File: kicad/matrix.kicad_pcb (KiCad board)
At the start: 2 copper layers, 110.7 x 76.2 mm, 20 parts, among them J1 Conn_01x08, U1 TLC59025, U10 P-FET, U11 P-FET, U2 74HC595, U3 74HC595, U4 P-FET, U5 P-FET, U6 P-FET, U7 P-FET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

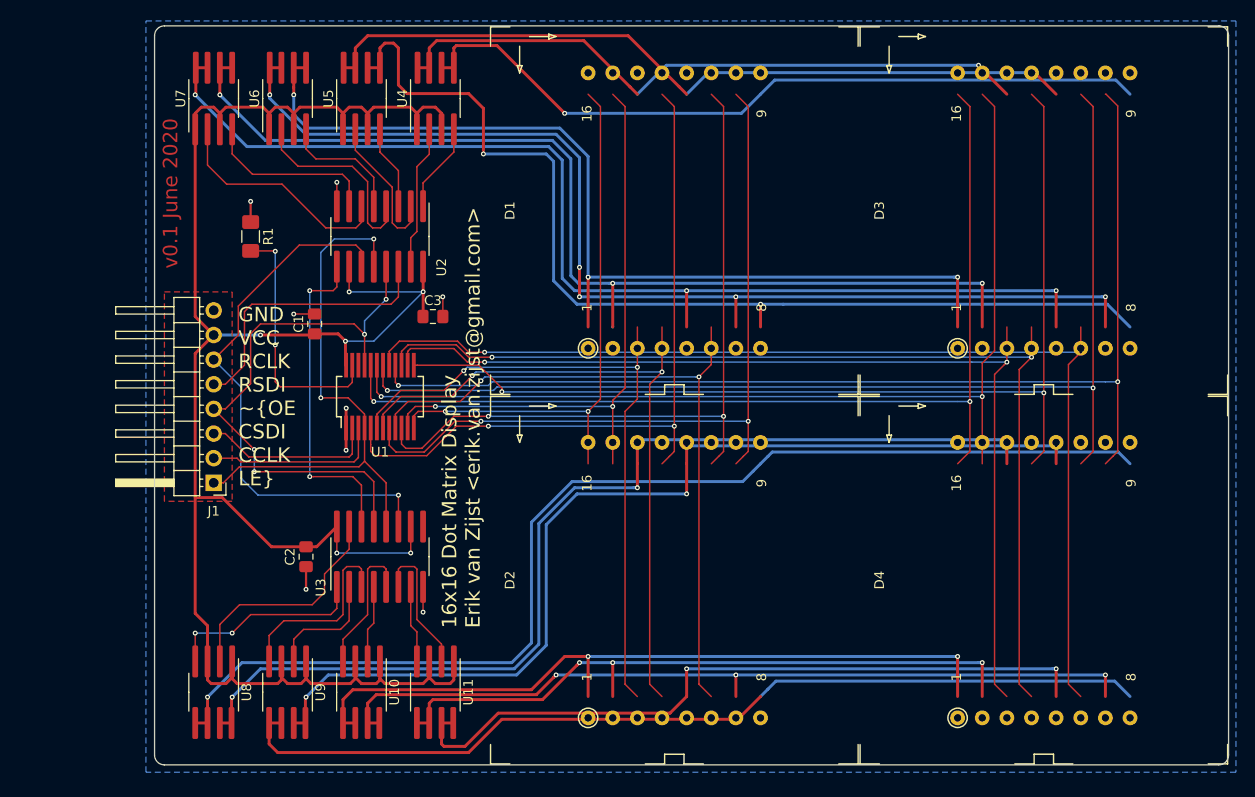
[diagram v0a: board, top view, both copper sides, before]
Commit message: Resize board and place components
Routing up next.
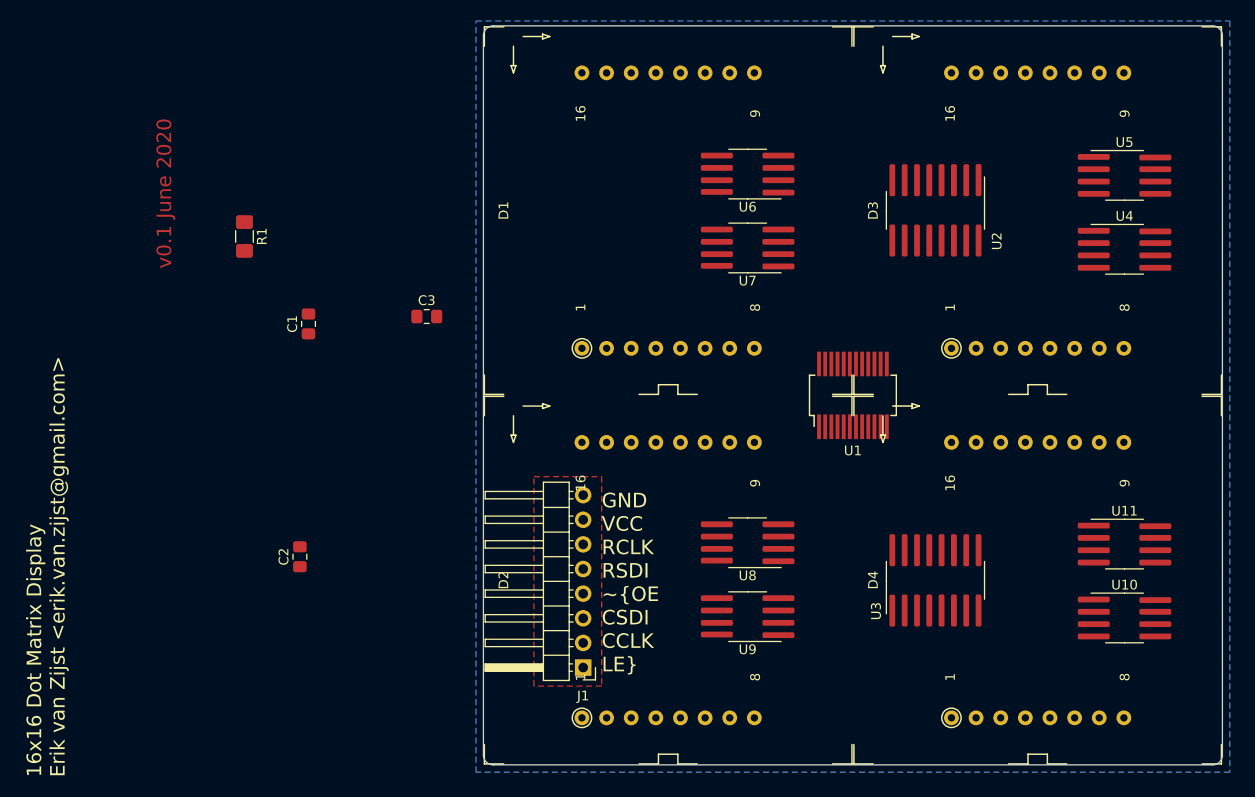
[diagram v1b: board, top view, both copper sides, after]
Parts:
- moved U5 79.1 mm to (218.4, 52.8), turned to 0 degrees
- moved U10 79.1 mm to (218.4, 98.4), turned to 0 degrees
- moved U4 72.7 mm to (218.4, 60.4), turned to 0 degrees
- moved U11 72.7 mm to (218.4, 90.8), turned to 0 degrees
- moved U2 57.3 mm to (198.9, 56.4)
- moved U3 57.3 mm to (198.9, 94.5)
- moved U7 57.2 mm to (179.5, 60.2), turned to 180 degrees
- moved U8 57.2 mm to (179.5, 90.6), turned to 180 degrees
- moved U1 48.8 mm to (190.4, 75.4)
- moved U6 48.1 mm to (179.5, 52.6), turned to 180 degrees
- moved U9 48.1 mm to (179.5, 98.3), turned to 180 degrees
- moved J1 42.6 mm to (162.6, 103.5)
- moved C2 0.64 mm to (133.3, 92.1)
- moved R1 0.64 mm to (127.6, 59.1)
- moved C1 0.63 mm to (134.2, 68.1)
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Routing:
- net VDD: track 223.1 -> 0.00 mm, vias 6 -> 0
- net /ROW9: track 117.3 -> 0.00 mm, vias 1 -> 0
- net /ROW8: track 115.8 -> 0.00 mm, vias 3 -> 0
- net /COL11: track 115.7 -> 0.00 mm, vias 2 -> 0
- net /COL13: track 114.9 -> 0.00 mm, vias 2 -> 0
- net /ROW6: track 113.6 -> 0.00 mm, vias 5 -> 0
- net /COL12: track 112.8 -> 0.00 mm, vias 2 -> 0
- net /ROW3: track 107.5 -> 0.00 mm, vias 2 -> 0
- net /ROW10: track 107.4 -> 0.00 mm, vias 4 -> 0
- net /ROW7: track 106.9 -> 0.00 mm, vias 3 -> 0
- net /COL10: track 106.3 -> 0.00 mm, vias 2 -> 0
- net /COL8: track 105.5 -> 0.00 mm, vias 2 -> 0
- net /COL14: track 104.5 -> 0.00 mm, vias 2 -> 0
- net /COL15: track 104.5 -> 0.00 mm, vias 2 -> 0
- net /ROW12: track 104.0 -> 0.00 mm, vias 4 -> 0
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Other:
- board size 110.7 x 76.2 mm -> 76.2 x 76.2 mm

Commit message: Widen capacitor footprint pads
Easier for hand soldering.
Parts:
- C1, C2, C3: footprint Capacitor_SMD:C_0805_2012Metric_Pad1.15x1.40mm_HandSolder -> local:C_0805_2012Metric_Pad1.15x1.40mm_widepads
- moved C2 57.8 mm to (191.1, 93.7)
- moved C3 56.9 mm to (203.3, 66.1), turned to 270 degrees
- moved C1 49.8 mm to (183.5, 75.4), turned to 270 degrees

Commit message: Widen resistor pads
For easier hand soldering.
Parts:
- R1: footprint Resistor_SMD:R_1206_3216Metric_Pad1.42x1.75mm_HandSolder -> local:R_1206_3216Metric_Pad1.42x1.75mm_widepads
- moved R1 97.1 mm to (223.4, 75.4), turned to 90 degrees
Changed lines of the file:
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@@
     (uvia_drill 0.1)
+  )
+  (module local:R_1206_3216Metric_Pad1.42x1.75mm_widepads (layer F.Cu)
+    (at 223.393 75.438 90)
+    (descr "Resistor SMD 1206 (3216 Metric), square (rectangular) end terminal, IPC_7351 nominal with elongated pad for handsoldering. (Body size source: http://www.tortai-tech.com/upload/download/2011102023233369053.pdf), generated with kicad-footprint-generator")
+    (tags "resistor handsolder")
+    (attr smd)
+    (fp_text reference R1 (at 0 -1.82 270) (layer F.SilkS)
+      (effects (font (size 1 1) (thickness 0.15)))
+    )
+    (fp_text value 2.2K (at 0 1.82 270) (layer F.Fab)
+      (effects (font (size 1 1) (thickness 0.15)))
+    )
+    (fp_line (start -1.6 0.8) (end -1.6 -0.8) (layer F.Fab) (width 0.1))
+    (fp_line (start -1.6 -0.8) (end 1.6 -0.8) (layer F.Fab) (width 0.1))
+    (fp_line (start 1.6 -0.8) (end 1.6 0.8) (layer F.Fab) (width 0.1))
+    (fp_line (start 1.6 0.8) (end -1.6 0.8) (layer F.Fab) (width 0.1))
+    (fp_line (start -0.602064 -0.91) (end 0.602064 -0.91) (layer F.SilkS) (width 0.12))
+    (fp_line (start -0.602064 0.91) (end 0.602064 0.91) (layer F.SilkS) (width 0.12))
+    (fp_line (start -3.85 1.12) (end -3.85 -1.12) (layer F.CrtYd) (width 0.05))
+    (fp_line (start -3.85 -1.12) (end 3.85 -1.12) (layer F.CrtYd) (width 0.05))
+    (fp_line (start 3.85 -1.12) (end 3.85 1.12) (layer F.CrtYd) (width 0.05))
+    (fp_line (start 3.85 1.12) (end -3.85 1.12) (layer F.CrtYd) (width 0.05))
+    (fp_text user %R (at 0 0 270) (layer F.Fab)
+      (effects (font (size 0.8 0.8) (thickness 0.12)))
+    )
+    (pad 1 smd roundrect (at -2.1875 0 90) (size 2.825 1.75) (layers F.Cu F.Paste F.Mask) (roundrect_rratio 0.175)
+      (net 36 GND))
+    (pad 2 smd roundrect (at 2.1875 0 90) (size 2.825 1.75) (layers F.Cu F.Paste F.Mask) (roundrect_rratio 0.175)
+      (net 39 "Net-(R1-Pad2)"))
+    (model ${KISYS3DMOD}/Resistor_SMD.3dshapes/R_1206_3216Metric.wrl
+      (at (xyz 0 0 0))
+      (scale (xyz 1 1 1))
+      (rotate (xyz 0 0 0))
+    )
   )
   (module local:C_0805_2012Metric_Pad1.15x1.40mm_widepads (layer F.Cu)
@@
       (at (xyz 0 0 0))
       (scale (xyz 1 1 1))
-      (rotate (xyz 0 0 0))
-    )
-  )
-  (module Resistor_SMD:R_1206_3216Metric_Pad1.42x1.75mm_HandSolder (layer F.Cu)
-    (at 127.635 59.055 270)
-    (descr "Resistor SMD 1206 (3216 Metric), square (rectangular) end terminal, IPC_7351 nominal with elongated pad for handsoldering. (Body size source: http://www.tortai-tech.com/upload/download/2011102023233369053.pdf), generated with kicad-footprint-generator")
-    (tags "resistor handsolder")
-    (attr smd)
-    (fp_text reference R1 (at 0 -1.82 90) (layer F.SilkS)
-      (effects (font (size 1 1) (thickness 0.15)))
-    )
-    (fp_text value 2.2K (at 0 1.82 90) (layer F.Fab)
-      (effects (font (size 1 1) (thickness 0.15)))
-    )
-    (fp_text user %R (at 0 0 90) (layer F.Fab)
-      (effects (font (size 0.8 0.8) (thickness 0.12)))
-    )
-    (fp_line (start 2.45 1.12) (end -2.45 1.12) (layer F.CrtYd) (width 0.05))
-    (fp_line (start 2.45 -1.12) (end 2.45 1.12) (layer F.CrtYd) (width 0.05))
-    (fp_line (start -2.45 -1.12) (end 2.45 -1.12) (layer F.CrtYd) (width 0.05))
-    (fp_line (start -2.45 1.12) (end -2.45 -1.12) (layer F.CrtYd) (width 0.05))
-    (fp_line (start -0.602064 0.91) (end 0.602064 0.91) (layer F.SilkS) (width 0.12))
-    (fp_line (start -0.602064 -0.91) (end 0.602064 -0.91) (layer F.SilkS) (width 0.12))
-    (fp_line (start 1.6 0.8) (end -1.6 0.8) (layer F.Fab) (width 0.1))
-    (fp_line (start 1.6 -0.8) (end 1.6 0.8) (layer F.Fab) (width 0.1))
-    (fp_line (start -1.6 -0.8) (end 1.6 -0.8) (layer F.Fab) (width 0.1))
-    (fp_line (start -1.6 0.8) (end -1.6 -0.8) (layer F.Fab) (width 0.1))
-    (pad 2 smd roundrect (at 1.4875 0 270) (size 1.425 1.75) (layers F.Cu F.Paste F.Mask) (roundrect_rratio 0.175439)
-      (net 39 "Net-(R1-Pad2)"))
-    (pad 1 smd roundrect (at -1.4875 0 270) (size 1.425 1.75) (layers F.Cu F.Paste F.Mask) (roundrect_rratio 0.175439)
-      (net 36 GND))
-    (model ${KISYS3DMOD}/Resistor_SMD.3dshapes/R_1206_3216Metric.wrl
-      (at (xyz 0 0 0))
-      (scale (xyz 1 1 1))

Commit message: Power net in place
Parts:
- moved C3 1.93 mm to (205.1, 65.3), turned to 0 degrees
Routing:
- net VDD: track 0.00 -> 171.6 mm

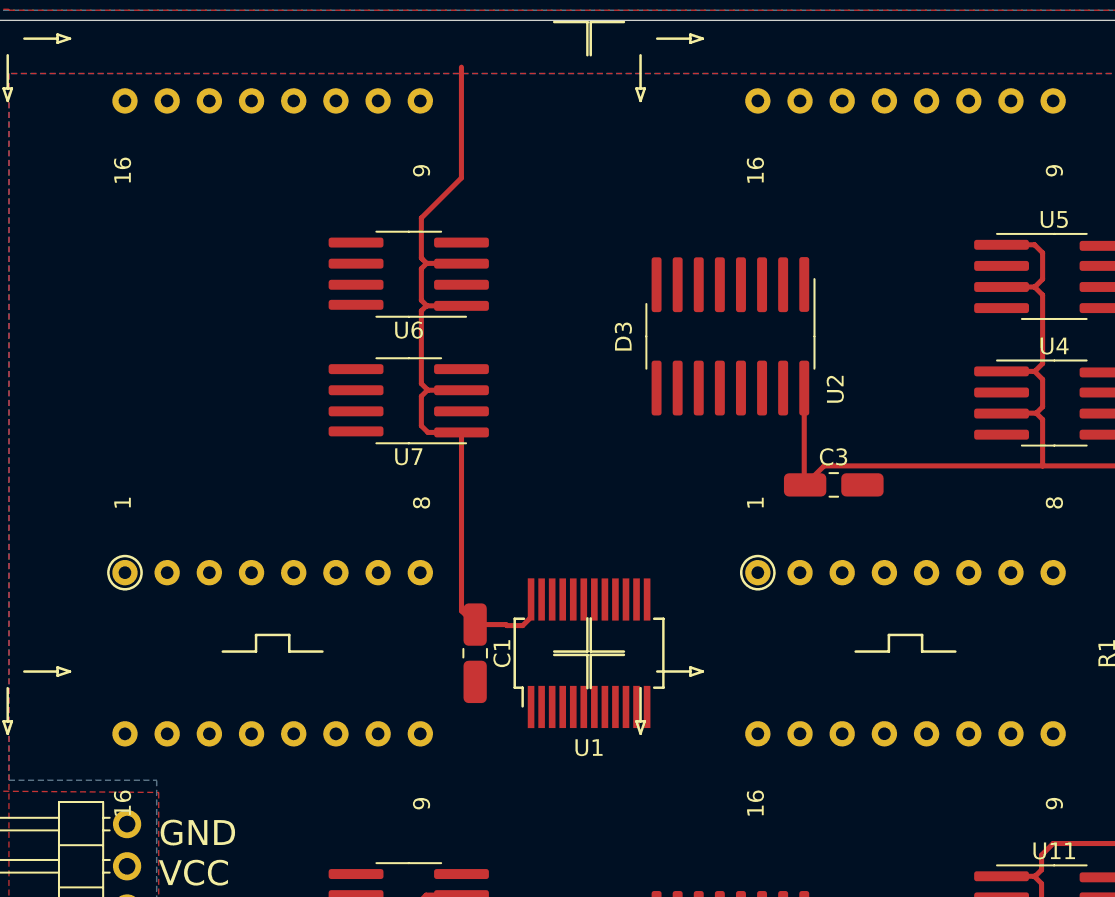
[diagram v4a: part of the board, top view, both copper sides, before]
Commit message: Wire up LED cathodes
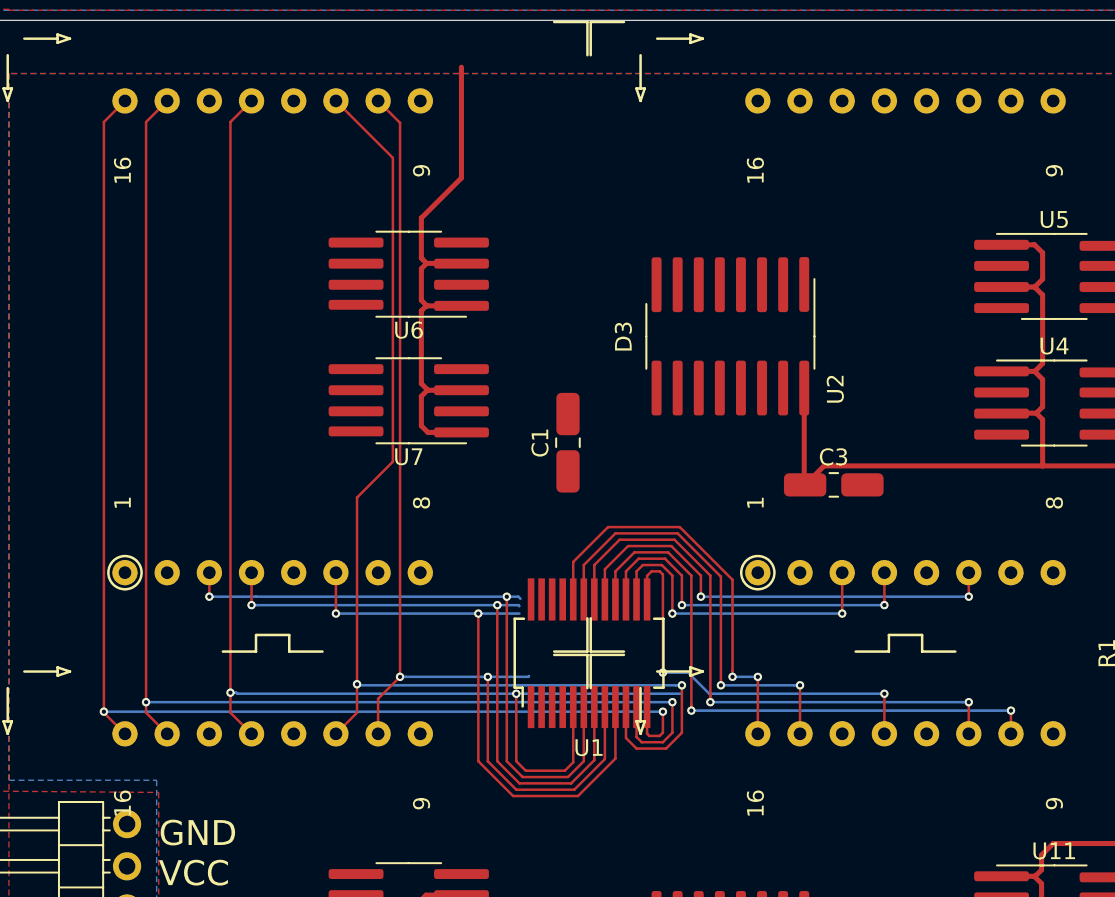
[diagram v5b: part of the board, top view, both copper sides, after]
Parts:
- moved C1 13.9 mm to (189.1, 62.8), turned to 90 degrees
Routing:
- net /COL0: track 0.00 -> 77.6 mm, vias 0 -> 2
- net /COL6: track 0.00 -> 77.0 mm, vias 0 -> 2
- net /COL7: track 0.00 -> 76.8 mm, vias 0 -> 2
- net /COL5: track 0.00 -> 69.3 mm, vias 0 -> 2
- net /COL3: track 0.00 -> 63.7 mm, vias 0 -> 2
- net /COL1: track 0.00 -> 38.8 mm, vias 0 -> 2
- net /COL2: track 0.00 -> 37.7 mm, vias 0 -> 2
- net /COL11: track 0.00 -> 36.1 mm, vias 0 -> 2
- net /COL13: track 0.00 -> 35.7 mm, vias 0 -> 2
- net /COL4: track 0.00 -> 35.6 mm, vias 0 -> 2
- net /COL12: track 0.00 -> 27.8 mm, vias 0 -> 2
- net /COL14: track 0.00 -> 26.4 mm, vias 0 -> 2
- net /COL15: track 0.00 -> 24.8 mm, vias 0 -> 2
- net /COL8: track 0.00 -> 24.7 mm, vias 0 -> 2
- net /COL10: track 0.00 -> 21.7 mm, vias 0 -> 2
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
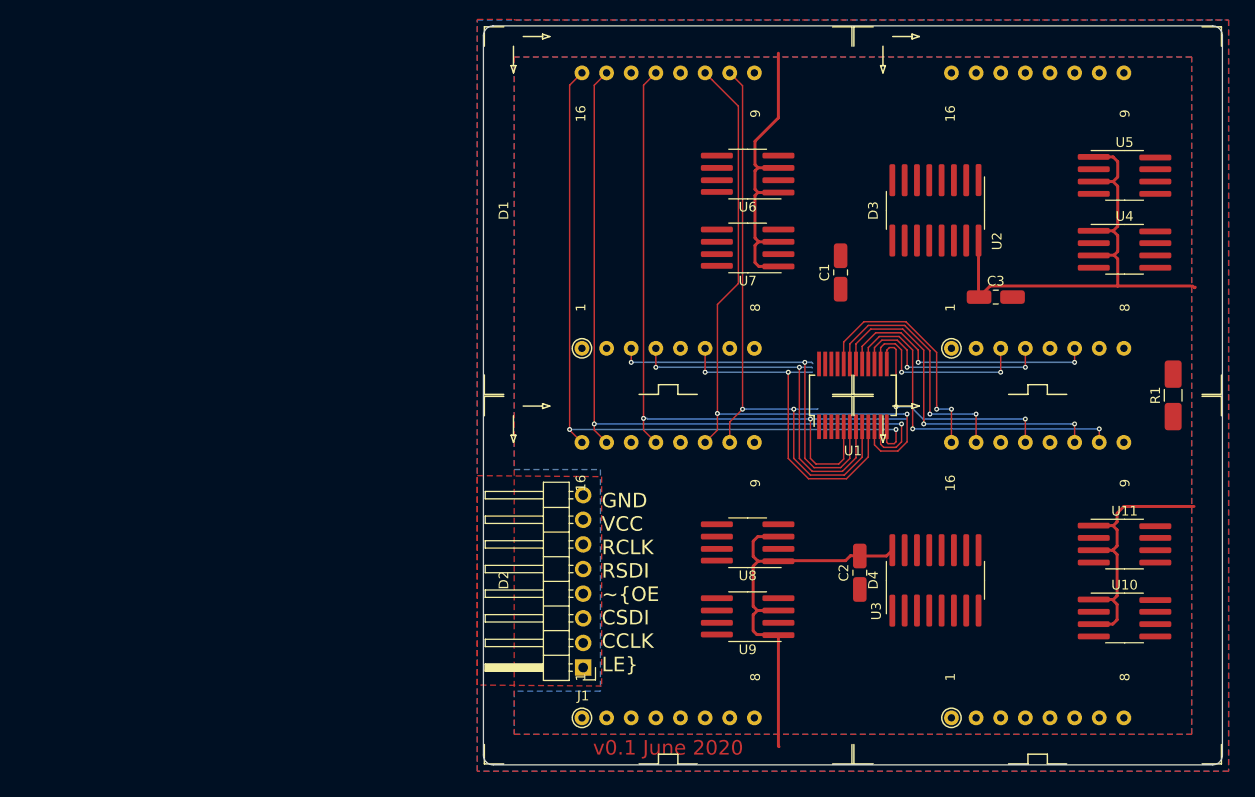
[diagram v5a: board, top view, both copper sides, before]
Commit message: Wire up most of the layout
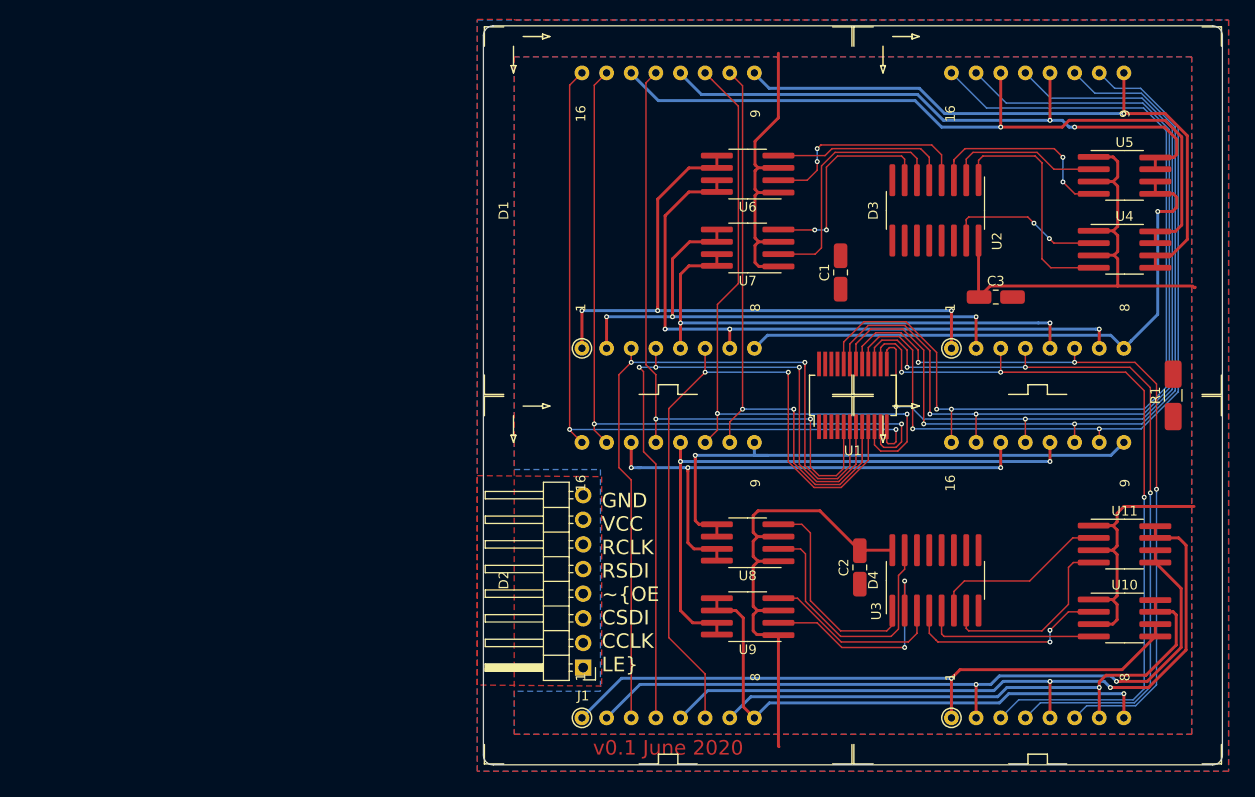
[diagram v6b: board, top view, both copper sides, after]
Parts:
- moved C2 0.55 mm to (191.1, 93.2)
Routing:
- net /ROW2: track 0.00 -> 79.0 mm, vias 0 -> 1
- net /ROW15: track 0.00 -> 77.3 mm, vias 0 -> 2
- net /ROW16: track 0.00 -> 74.8 mm, vias 0 -> 2
- net /COL15: track 24.8 -> 99.0 mm
- net /COL14: track 26.4 -> 96.5 mm
- net /ROW6: track 0.00 -> 68.0 mm, vias 0 -> 3
- net /ROW13: track 0.00 -> 67.9 mm, vias 0 -> 1
- net /ROW1: track 0.00 -> 67.5 mm, vias 0 -> 1
- net /ROW5: track 0.00 -> 66.1 mm, vias 0 -> 3
- net /ROW4: track 0.00 -> 64.0 mm, vias 0 -> 2
- net /ROW12: track 0.00 -> 62.9 mm, vias 0 -> 2
- net /COL9: track 19.2 -> 81.6 mm, vias 2 -> 3
- net /ROW3: track 0.00 -> 61.6 mm, vias 0 -> 1
- net /COL8: track 24.7 -> 85.6 mm
- net /ROW14: track 0.00 -> 59.2 mm, vias 0 -> 1
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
